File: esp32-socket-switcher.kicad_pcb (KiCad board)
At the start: 2 copper layers, 82.2 x 40.5 mm, 40 parts, among them IC1 ADP2301AUJZ-R7, J1 USB4110GFA, K1 G5CA-1A DC5, Q1 SS8050-G, Q2 SS8050-G, Q3 CSD17575Q3T, U2 ESP32-WROOM-32E-H4, U5 CP2102N-A02-GQFN24R

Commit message: mains to relay lable
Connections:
- K1 pad 3: unconnected-(K1-Pad3) -> /AC_LIVE_SWITCHED
- K1 pad 4: unconnected-(K1-Pad4) -> /AC_LIVE
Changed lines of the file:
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@@
   (net 62 "unconnected-(U5-SUSPEND-Pad17)")
   (net 63 "unconnected-(U5-~{CTS}-Pad18)")
-  (net 64 "unconnected-(K1-Pad3)")
-  (net 65 "unconnected-(U5-NC-Pad10)")
-  (net 66 "unconnected-(U5-NC-Pad16)")
-  (net 67 "/ESP32/ESP32_MOSI")
-  (net 68 "unconnected-(K1-Pad4)")
-  (net 69 "Net-(PS1-AC(L))")
-  (net 70 "/ESP32/RELAY_OUT")
-  (net 71 "/ESP32/SWITCH_IN")
-  (net 72 "Net-(PS1-+V(CAP))")
-  (net 73 "Net-(Q3-G)")
+  (net 64 "unconnected-(U5-NC-Pad10)")
+  (net 65 "unconnected-(U5-NC-Pad16)")
+  (net 66 "/ESP32/ESP32_MOSI")
+  (net 67 "Net-(PS1-AC(L))")
+  (net 68 "/ESP32/RELAY_OUT")
+  (net 69 "/ESP32/SWITCH_IN")
+  (net 70 "Net-(PS1-+V(CAP))")
+  (net 71 "Net-(Q3-G)")
+  (net 72 "/AC_LIVE_SWITCHED")
+  (net 73 "/AC_LIVE")
   (footprint "esp32-socket-switcher:SOD2512X110N" (layer "F.Cu")
     (at 58.805 72.635)
@@
       (stroke (width 0.1) (type solid)) (layer "F.Fab"))
     (pad "1" smd roundrect (at -0.375 0) (size 0.45 0.5) (layers "F.Cu" "F.Paste" "F.Mask") (roundrect_rratio 0.25)
-      (net 70 "/ESP32/RELAY_OUT") (pintype "passive") (solder_mask_margin 0.0508))
+      (net 68 "/ESP32/RELAY_OUT") (pintype "passive") (solder_mask_margin 0.0508))
     (pad "2" smd roundrect (at 0.375 0) (size 0.45 0.5) (layers "F.Cu" "F.Paste" "F.Mask") (roundrect_rratio 0.25)
-      (net 73 "Net-(Q3-G)") (pintype "passive") (solder_mask_margin 0.0508))
+      (net 71 "Net-(Q3-G)") (pintype "passive") (solder_mask_margin 0.0508))
     (model "${KICAD6_3DMODEL_DIR}/Resistor_SMD.3dshapes/R_0402_1005Metric.wrl"
       (offset (xyz 0 0 0))
@@
       (net 20 "unconnected-(U2-IO33-Pad9)") (pinfunction "IO33") (pintype "input"))
     (pad "10" smd rect (at -8.75 3.18 270) (size 1.5 0.9) (layers "F.Cu" "F.Paste" "F.Mask")
-      (net 70 "/ESP32/RELAY_OUT") (pinfunction "IO25") (pintype "input"))
+      (net 68 "/ESP32/RELAY_OUT") (pinfunction "IO25") (pintype "input"))
     (pad "11" smd rect (at -8.75 4.45 270) (size 1.5 0.9) (layers "F.Cu" "F.Paste" "F.Mask")
-      (net 71 "/ESP32/SWITCH_IN") (pinfunction "IO26") (pintype "input"))
+      (net 69 "/ESP32/SWITCH_IN") (pinfunction "IO26") (pintype "input"))
     (pad "12" smd rect (at -8.75 5.72 270) (size 1.5 0.9) (layers "F.Cu" "F.Paste" "F.Mask")
       (net 23 "unconnected-(U2-IO27-Pad12)") (pinfunction "IO27") (pintype "input"))
@@
       (net 40 "unconnected-(U2-IO22-Pad36)") (pinfunction "IO22") (pintype "input"))
     (pad "37" smd rect (at 8.75 -6.98 270) (size 1.5 0.9) (layers "F.Cu" "F.Paste" "F.Mask")
-      (net 67 "/ESP32/ESP32_MOSI") (pinfunction "IO23") (pintype "input"))
+      (net 66 "/ESP32/ESP32_MOSI") (pinfunction "IO23") (pintype "input"))
     (pad "38" smd rect (at 8.75 -8.25 270) (size 1.5 0.9) (layers "F.Cu" "F.Paste" "F.Mask")
       (net 2 "GND") (pinfunction "GND") (pintype "input"))
@@
       (stroke (width 0.2) (type solid)) (fill none) (layer "F.Fab"))
     (pad "1" thru_hole rect (at -6.775 0) (size 2.77 2.77) (drill 2.27) (layers "*.Cu" "*.Mask")
-      (net 69 "Net-(PS1-AC(L))") (pinfunction "AC(L)") (pintype "input") (solder_mask_margin 0.102))
+      (net 67 "Net-(PS1-AC(L))") (pinfunction "AC(L)") (pintype "input") (solder_mask_margin 0.102))
     (pad "2" thru_hole circle (at -1.695 0) (size 2.77 2.77) (drill 2.27) (layers "*.Cu" "*.Mask")
-      (net 72 "Net-(PS1-+V(CAP))") (pinfunction "+V(CAP)") (pintype "passive") (solder_mask_margin 0.102))
+      (net 70 "Net-(PS1-+V(CAP))") (pinfunction "+V(CAP)") (pintype "passive") (solder_mask_margin 0.102))
     (pad "3" thru_hole circle (at 3.385 0) (size 2.77 2.77) (drill 2.27) (layers "*.Cu" "*.Mask")
       (net 2 "GND") (pinfunction "AC(N)/-VO") (pintype "bidirectional") (solder_mask_margin 0.102))
@@
       (net 22 "Net-(D7-A)") (pinfunction "2") (pintype "unspecified"))
     (pad "3" thru_hole oval (at 12.7 10.16 180) (size 2.507996 1.507998) (drill oval 2 1) (layers "*.Cu" "*.Mask")
-      (net 64 "unconnected-(K1-Pad3)") (pinfunction "3") (pintype "unspecified"))
+      (net 72 "/AC_LIVE_SWITCHED") (pinfunction "3") (pintype "unspecified"))
     (pad "4" thru_hole oval (at 12.7 0 180) (size 2.507996 1.507998) (drill oval 2 1) (layers "*.Cu" "*.Mask")
-      (net 68 "unconnected-(K1-Pad4)") (pinfunction "4") (pintype "unspecified"))
+      (net 73 "/AC_LIVE") (pinfunction "4") (pintype "unspecified"))
     (model "${KIPRJMOD}/3dModels/G5CA_1A.step"
       (offset (xyz 0 0 0))
@@
       (net 2 "GND") (pinfunction "S") (pintype "passive") (solder_mask_margin 0.0508))
     (pad "2" smd oval (at -1.475 0.965 90) (size 0.35 0.9) (layers "F.Cu" "F.Paste" "F.Mask")
-      (net 73 "Net-(Q3-G)") (pinfunction "G") (pintype "input") (solder_mask_margin 0.0508))
+      (net 71 "Net-(Q3-G)") (pinfunction "G") (pintype "input") (solder_mask_margin 0.0508))
     (pad "3" smd rect (at 0.375 -0.01 180) (size 1.75 2.45) (layers "F.Cu" "F.Mask")
       (net 22 "Net-(D7-A)") (pinfunction "D") (pintype "passive") (solder_mask_margin 0.0508))
@@
       (net 9 "Net-(U5-~{RST})") (pinfunction "~{RST}") (pintype "bidirectional") (solder_mask_margin 0.102))
     (pad "10" smd roundrect (at 0.25 -1.935 180) (size 0.84 0.26) (layers "B.Cu" "B.Paste" "B.Mask") (roundrect_rratio 0.03)
-      (net 65 "unconnected-(U5-NC-Pad10)") (pinfunction "NC") (pintype "no_connect") (solder_mask_margin 0.102))
+      (net 64 "unconnected-(U5-NC-Pad10)") (pinfunction "NC") (pintype "no_connect") (solder_mask_margin 0.102))
     (pad "11" smd roundrect (at 0.75 -1.935 180) (size 0.84 0.26) (layers "B.Cu" "B.Paste" "B.Mask") (roundrect_rratio 0.03)
       (net 54 "unconnected-(U5-GPIO.3{slash}WAKEUP-Pad11)") (pinfunction "GPIO.3/WAKEUP") (pintype "bidirectional+no_connect") (solder_mask_margin 0.102))
@@
       (net 61 "unconnected-(U5-SUSPENDB-Pad15)") (pinfunction "SUSPENDB") (pintype "output+no_connect") (solder_mask_margin 0.102))
     (pad "16" smd roundrect (at 1.935 0.25 270) (size 0.84 0.26) (layers "B.Cu" "B.Paste" "B.Mask") (roundrect_rratio 0.03)
-      (net 66 "unconnected-(U5-NC-Pad16)") (pinfunction "NC") (pintype "no_connect") (solder_mask_margin 0.102))
+      (net 65 "unconnected-(U5-NC-Pad16)") (pinfunction "NC") (pintype "no_connect") (solder_mask_margin 0.102))
     (pad "17" smd roundrect (at 1.935 0.75 270) (size 0.84 0.26) (layers "B.Cu" "B.Paste" "B.Mask") (roundrect_rratio 0.03)
       (net 62 "unconnected-(U5-SUSPEND-Pad17)") (pinfunction "SUSPEND") (pintype "output+no_connect") (solder_mask_margin 0.102))

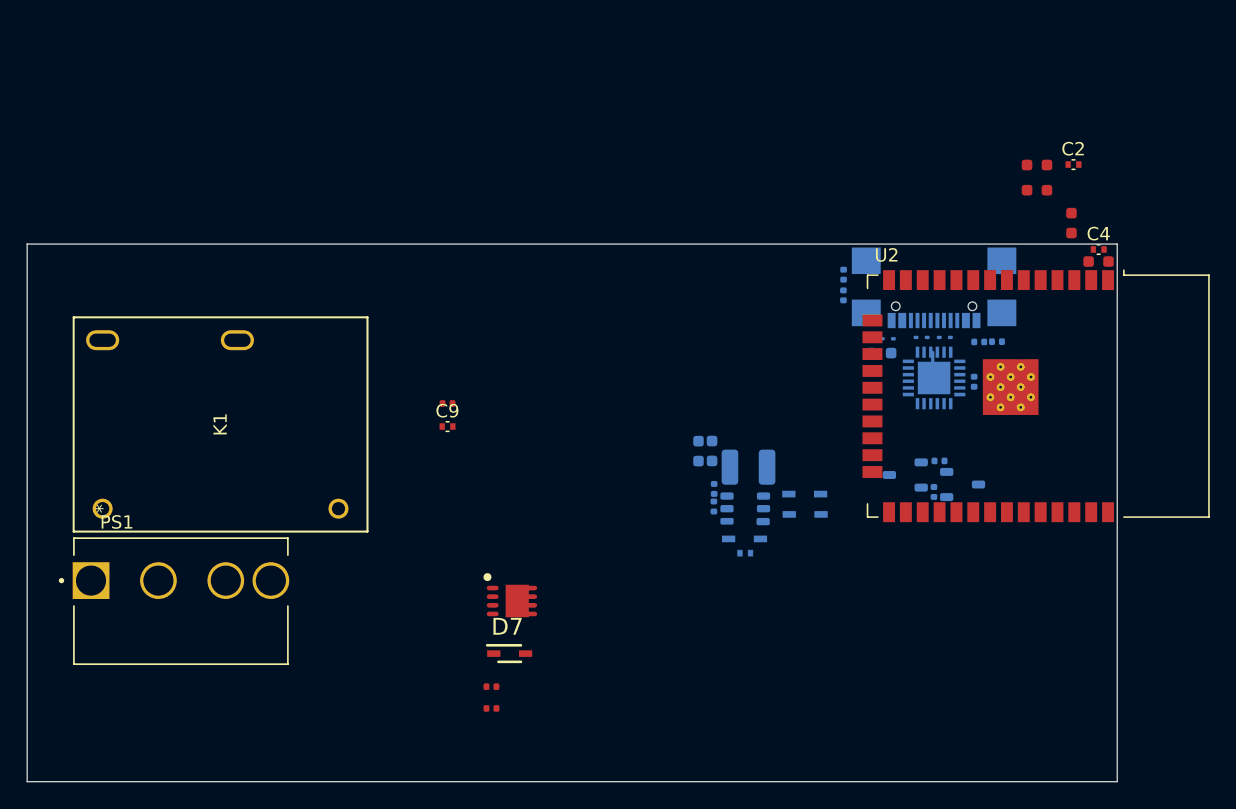
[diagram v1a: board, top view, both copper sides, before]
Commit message: some routing. need to add the things
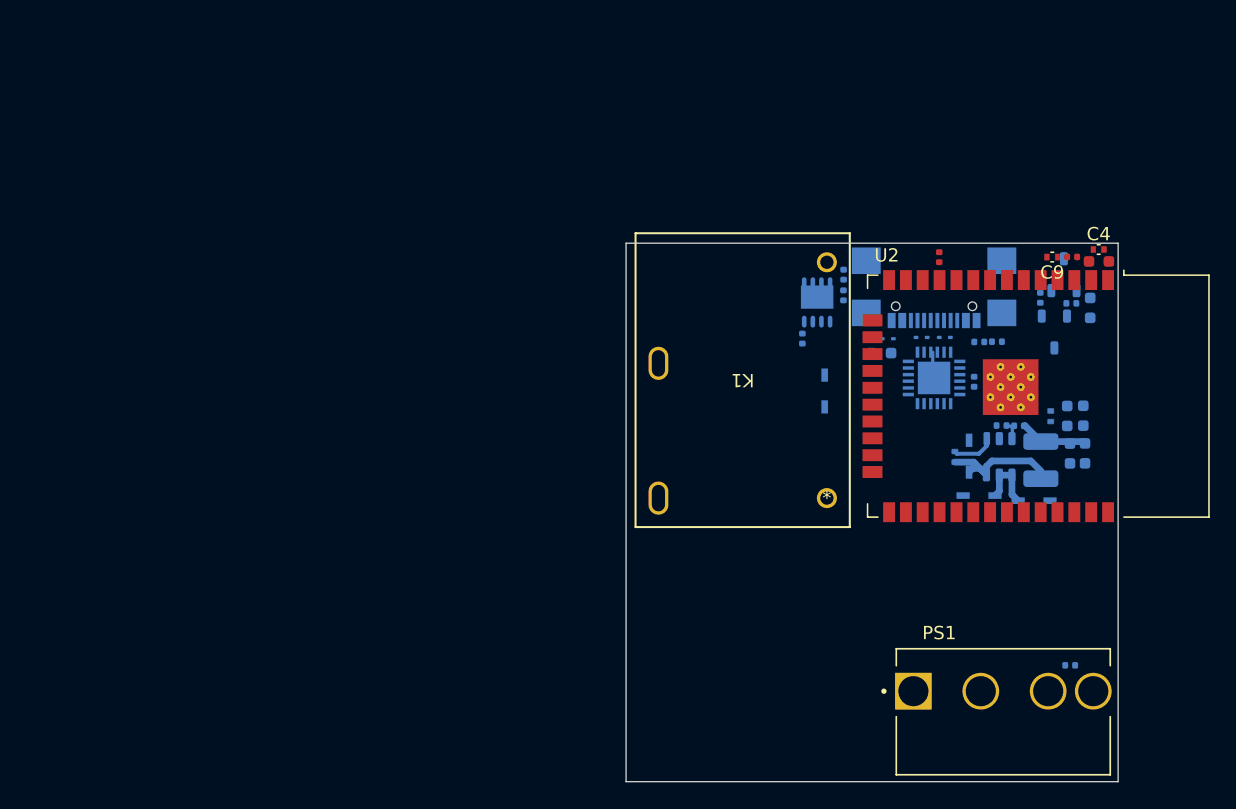
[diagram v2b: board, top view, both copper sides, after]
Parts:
- added R13: 10k, esp32-socket-switcher:R_0402_1005Metric, F.Cu at (91.2, 42.8)
- C1, C10, C2, C3, D7, Q3, R10, R12: moved to B.Cu
- moved PS1 62.6 mm to (96.0, 75.5)
- moved K1 54.6 mm to (82.7, 60.9), turned to 180 degrees
- moved R6 48.4 mm to (101.2, 42.7)
- moved C9 47.3 mm to (99.7, 42.7), turned to 180 degrees
- moved R10 43.7 mm to (101.1, 73.5)
- moved R12 36.4 mm to (80.9, 48.9), turned to 90 degrees
- moved Q3 32.2 mm to (82.0, 46.1), turned to 90 degrees
- moved D7 30.9 mm to (82.5, 52.8), turned to 90 degrees
- moved C7 29.1 mm to (102.2, 57.5), turned to -90 degrees
- moved C8 27.0 mm to (101.0, 57.5), turned to -90 degrees
- moved R5 23.5 mm to (97.2, 55.5), turned to 0 degrees
- moved R11 22.5 mm to (95.9, 55.4), turned to 0 degrees
- moved L1 22.0 mm to (98.8, 58.0), turned to 90 degrees
- moved IC1 19.5 mm to (95.7, 57.8), turned to -90 degrees
- moved C2 19.0 mm to (99.6, 54.7), turned to 90 degrees
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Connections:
- U2 pad 11: /ESP32/SWITCH_IN -> /SWITCH_IN
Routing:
- net Net-(D1-K): track 0.00 -> 10.2 mm
- net 3v3: track 0.00 -> 5.15 mm
- net /3V3-Supply/VIN: track 0.00 -> 4.75 mm
- net Net-(IC1-BST): track 0.00 -> 3.28 mm
- net /3V3-Supply/FB: track 0.00 -> 1.62 mm
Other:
- board size 82.2 x 40.5 mm -> 37.1 x 40.6 mm

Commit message: added screw terms. think i need a barrier block instead...
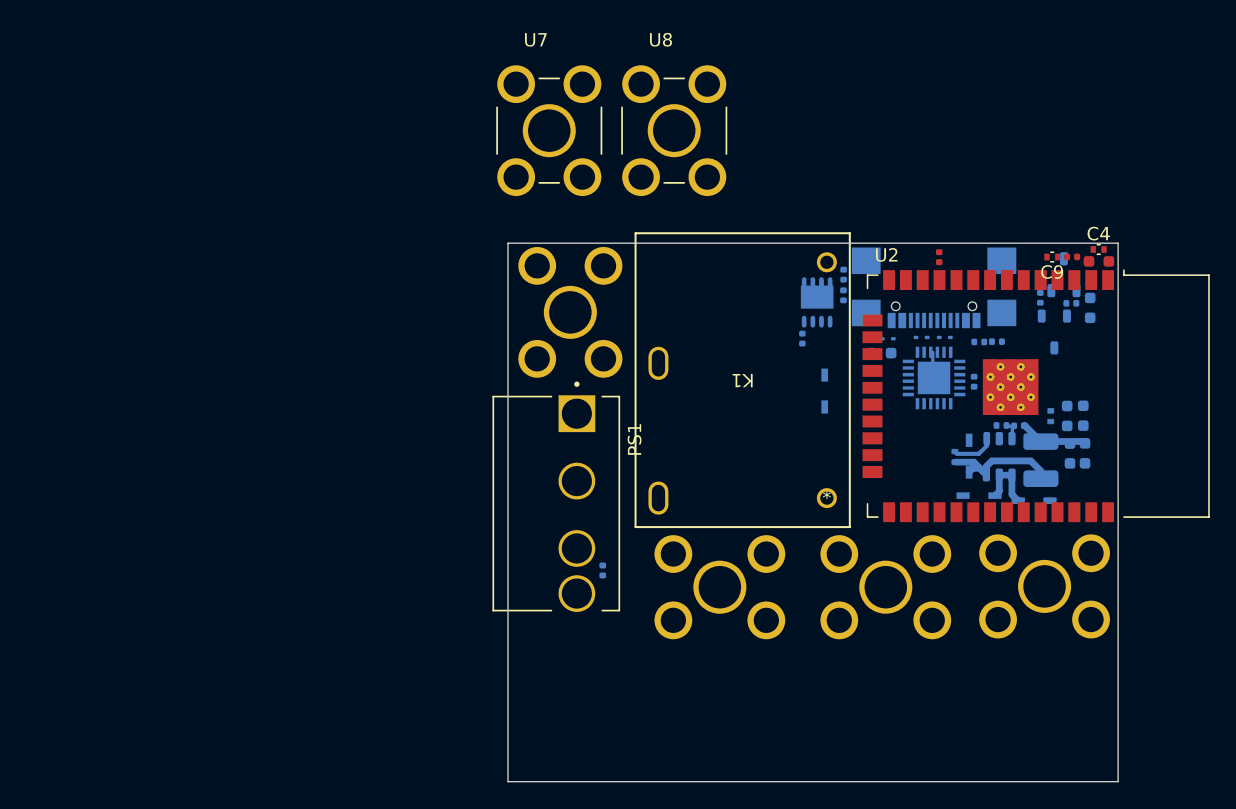
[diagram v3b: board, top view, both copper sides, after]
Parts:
- added U1: ~, esp32-socket-switcher:KEYSTONE_7770, B.Cu at (74.7, 67.6)
- added U3: ~, esp32-socket-switcher:KEYSTONE_7770, B.Cu at (87.2, 67.6)
- added U4: ~, esp32-socket-switcher:KEYSTONE_7770, B.Cu at (63.4, 46.9)
- added U6: ~, esp32-socket-switcher:KEYSTONE_7770, B.Cu at (99.1, 67.6)
- added U7: ~, esp32-socket-switcher:KEYSTONE_7770, F.Cu at (61.8, 33.2)
- added U8: ~, esp32-socket-switcher:KEYSTONE_7770, F.Cu at (71.2, 33.2)
- moved R10 36.0 mm to (65.8, 66.4), turned to -90 degrees
- moved PS1 35.1 mm to (63.9, 61.3), turned to -90 degrees
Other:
- board size 37.1 x 40.6 mm -> 46 x 40.6 mm

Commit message: swtiched to barrier block
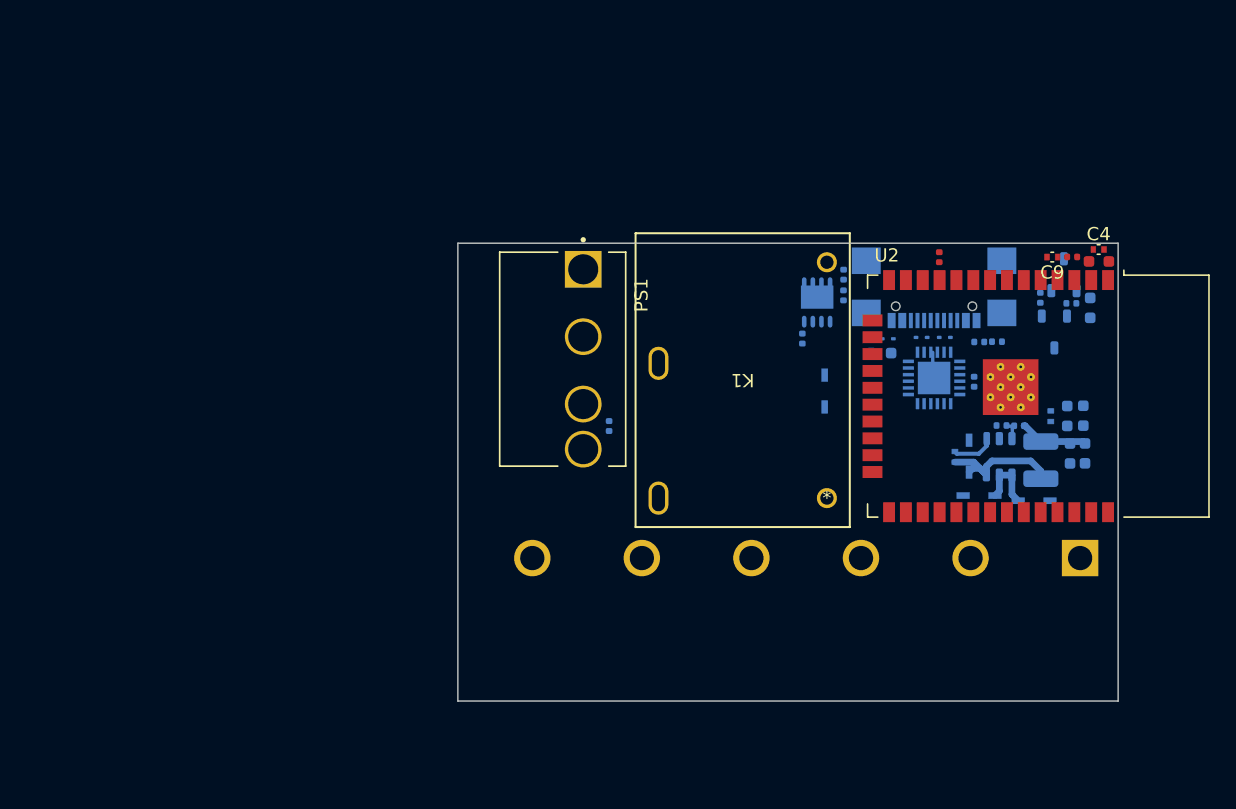
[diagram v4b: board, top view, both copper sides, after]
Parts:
- removed U1, U3, U4, U6, U7, U8: ~, esp32-socket-switcher:KEYSTONE_7770
- added J2: 4DB-P108-06, esp32-socket-switcher:TE_2-1437667-9, B.Cu at (81.2, 65.4)
- moved R10 10.9 mm to (66.3, 55.5)
- moved PS1 10.9 mm to (64.3, 50.4)
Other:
- board size 46 x 40.6 mm -> 49.8 x 34.5 mm

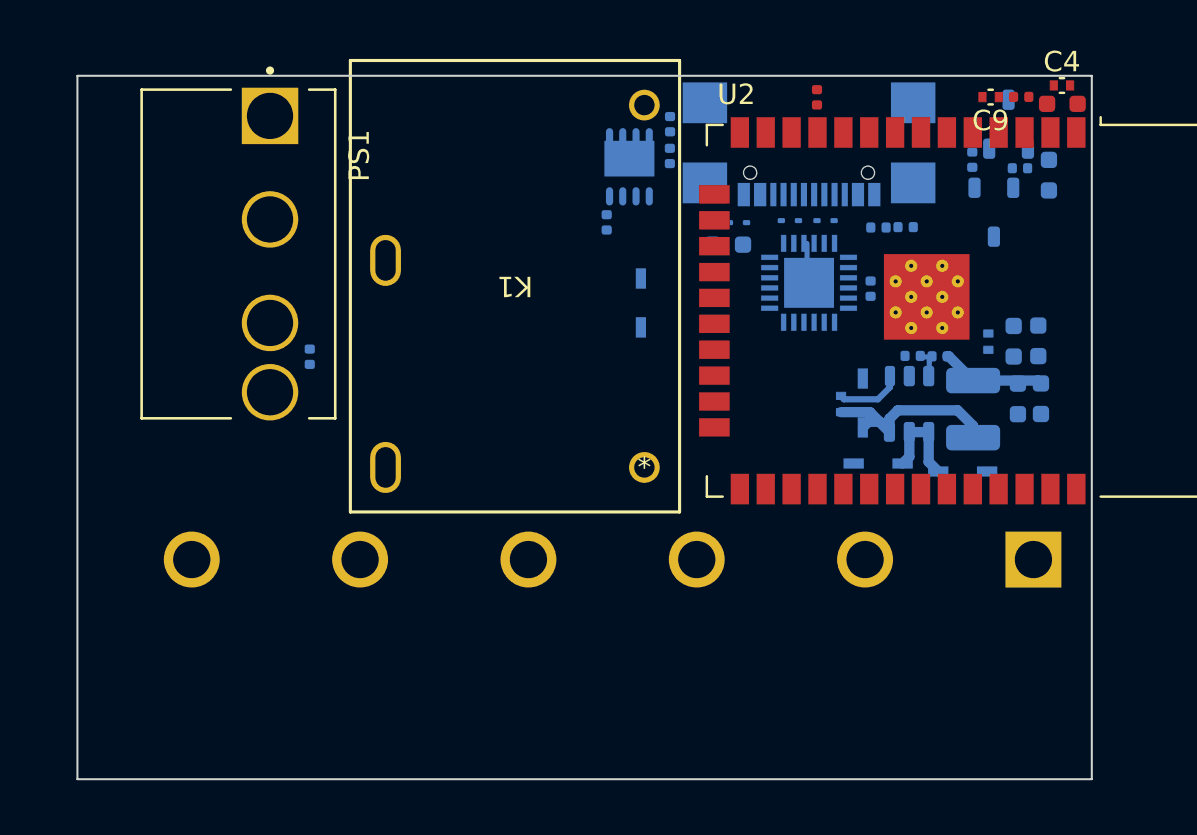
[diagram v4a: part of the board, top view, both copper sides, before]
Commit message: added caps and placed them
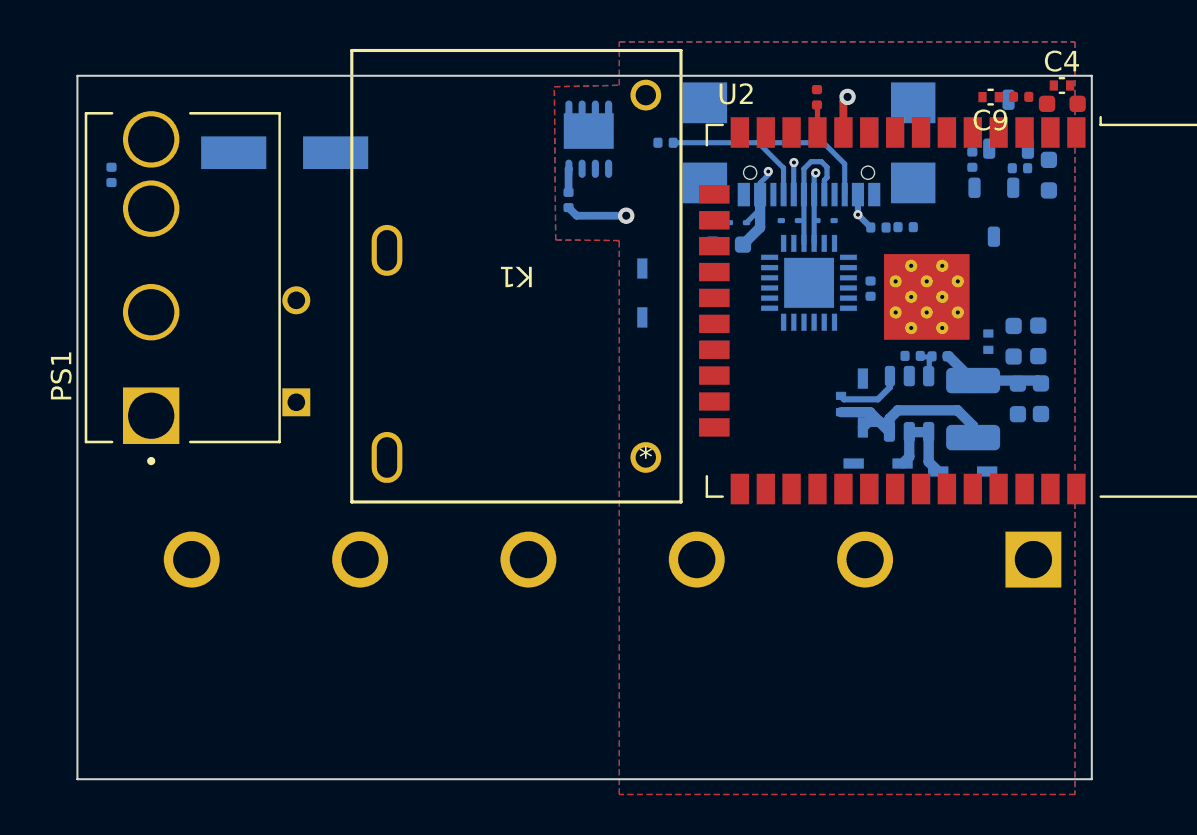
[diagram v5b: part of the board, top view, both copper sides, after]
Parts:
- removed R8: 5.1k, esp32-socket-switcher:R_0402_1005Metric
- added C12: 220uF/16V, esp32-socket-switcher:CAP_EEEFK1C221XP, B.Cu at (65.1, 45.5)
- added C13: 10uF/400V: 165-264VAC, esp32-socket-switcher:U1-S_NCH, B.Cu at (65.6, 57.7)
- moved R10 13.2 mm to (56.6, 46.6), turned to 90 degrees
- moved PS1 5.94 mm to (58.5, 51.6), turned to 90 degrees
- moved Q3 2.41 mm to (80.0, 44.8)
- moved R12 2.17 mm to (79.0, 47.8)
- moved R7 0.94 mm to (83.8, 45.0), turned to 0 degrees
- moved D7 0.49 mm to (82.6, 52.4)
- moved K1 0.49 mm to (82.8, 60.4)
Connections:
- J1 pad B5: Net-(J1-CC2) -> Net-(J1-CC1)
- R4 pad 2: /ESP32/VUSB -> /VUSB
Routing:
- net /ESP32/RELAY_OUT: track 0.00 -> 18.1 mm, vias 0 -> 2
- net /VUSB: track 0.00 -> 13.6 mm, vias 0 -> 2
- net Net-(J1-CC1): track 0.00 -> 13.4 mm
- net /D+: track 0.00 -> 6.45 mm
- net /D-: track 0.00 -> 6.35 mm, vias 0 -> 2
- net GND: track 2.25 -> 0.00 mm
- net /SWITCH_IN: track 0.00 -> 1.36 mm
- net Net-(Q3-G): track 0.00 -> 1.17 mm
- added copper zone on B.Cu, net GND
- added copper zone on F.Cu, net GND
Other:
- copper layers 2 -> 4
